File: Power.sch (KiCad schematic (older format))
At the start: 0 parts

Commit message: Understanding the Power Protection And Filtering Module
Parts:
- added C? (x2): C, symbol C
- added F? (x4): FUSE, symbol FUSE
- added L? (x2): INDUCTOR, symbol INDUCTOR
- added P?: CONN_12X2, symbol CONN_12X2
- added R?: R, symbol R
- added SW?: SWITCH_INV, symbol SWITCH_INV
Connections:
- net labels added: +12P, +12V, +3.3V, +5V, -12P, -12V, GND
- wire segments 0 -> 39

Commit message: Revisting the Current/Fan Module
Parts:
- removed F? (x4): FUSE, symbol FUSE
- added TH? (x4): THERMISTOR, symbol THERMISTOR
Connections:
- net labels added: +12C
- wire segments 39 -> 40
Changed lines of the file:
@@
 $Descr A4 11693 8268
 encoding utf-8
-Sheet 5 9
+Sheet 4 9
 Title ""
 Date ""
@@
 $EndComp
 $Comp
-L FUSE F?
-U 1 1 52F2232F
-P 3350 2100
-F 0 "F?" H 3450 2150 40  0000 C CNN
-F 1 "FUSE" H 3250 2050 40  0000 C CNN
-F 2 "" H 3350 2100 60  0000 C CNN
-F 3 "" H 3350 2100 60  0000 C CNN
-	1    3350 2100
-	1    0    0    -1
-$EndComp
-$Comp
-L FUSE F?
-U 1 1 52F2234B
-P 3950 2300
-F 0 "F?" H 4050 2350 40  0000 C CNN
-F 1 "FUSE" H 3850 2250 40  0000 C CNN
-F 2 "" H 3950 2300 60  0000 C CNN
-F 3 "" H 3950 2300 60  0000 C CNN
-	1    3950 2300
-	1    0    0    -1
-$EndComp
-$Comp
-L FUSE F?
-U 1 1 52F22356
-P 4550 2500
-F 0 "F?" H 4650 2550 40  0000 C CNN
-F 1 "FUSE" H 4450 2450 40  0000 C CNN
-F 2 "" H 4550 2500 60  0000 C CNN
-F 3 "" H 4550 2500 60  0000 C CNN
-	1    4550 2500
-	1    0    0    -1
-$EndComp
-$Comp
-L FUSE F?
-U 1 1 52F22361
-P 5150 2700
-F 0 "F?" H 5250 2750 40  0000 C CNN
-F 1 "FUSE" H 5050 2650 40  0000 C CNN
-F 2 "" H 5150 2700 60  0000 C CNN
-F 3 "" H 5150 2700 60  0000 C CNN
-	1    5150 2700
-	1    0    0    -1
-$EndComp
-$Comp
 L SWITCH_INV SW?
 U 1 1 52F2236E
@@
 	9850 3700 9850 3850
 Connection ~ 9100 3700
+Wire Wire Line
+	2950 2500 2950 1750
+Connection ~ 2950 2500
+$Comp
+L +12C #PWR?
+U 1 1 52F834A0
+P 2950 1750
+F 0 "#PWR?" H 2950 1720 30  0001 C CNN
+F 1 "+12C" H 2950 1860 40  0000 C CNN
+F 2 "" H 2950 1750 60  0000 C CNN
+F 3 "" H 2950 1750 60  0000 C CNN
+	1    2950 1750
+	1    0    0    -1
+$EndComp
+$Comp
+L THERMISTOR TH?
+U 1 1 52F839EB
+P 3350 2100
+F 0 "TH?" V 3450 2150 50  0000 C CNN
+F 1 "THERMISTOR" V 3250 2100 50  0000 C CNN
+F 2 "" H 3350 2100 60  0000 C CNN
+F 3 "" H 3350 2100 60  0000 C CNN
+	1    3350 2100
+	0    -1   -1   0
+$EndComp
+$Comp
+L THERMISTOR TH?
+U 1 1 52F83A04
+P 3950 2300
+F 0 "TH?" V 4050 2350 50  0000 C CNN
+F 1 "THERMISTOR" V 3850 2300 50  0000 C CNN
+F 2 "" H 3950 2300 60  0000 C CNN
+F 3 "" H 3950 2300 60  0000 C CNN
+	1    3950 2300
+	0    -1   -1   0
+$EndComp
+$Comp
+L THERMISTOR TH?
+U 1 1 52F83A18
+P 4550 2500
+F 0 "TH?" V 4650 2550 50  0000 C CNN
+F 1 "THERMISTOR" V 4450 2500 50  0000 C CNN
+F 2 "" H 4550 2500 60  0000 C CNN
+F 3 "" H 4550 2500 60  0000 C CNN
+	1    4550 2500
+	0    -1   -1   0
+$EndComp
+$Comp
+L THERMISTOR TH?
+U 1 1 52F83A2C
+P 5150 2700
+F 0 "TH?" V 5250 2750 50  0000 C CNN
+F 1 "THERMISTOR" V 5050 2700 50  0000 C CNN
+F 2 "" H 5150 2700 60  0000 C CNN
+F 3 "" H 5150 2700 60  0000 C CNN
+	1    5150 2700
+	0    -1   -1   0
+$EndComp
 $EndSCHEMATC

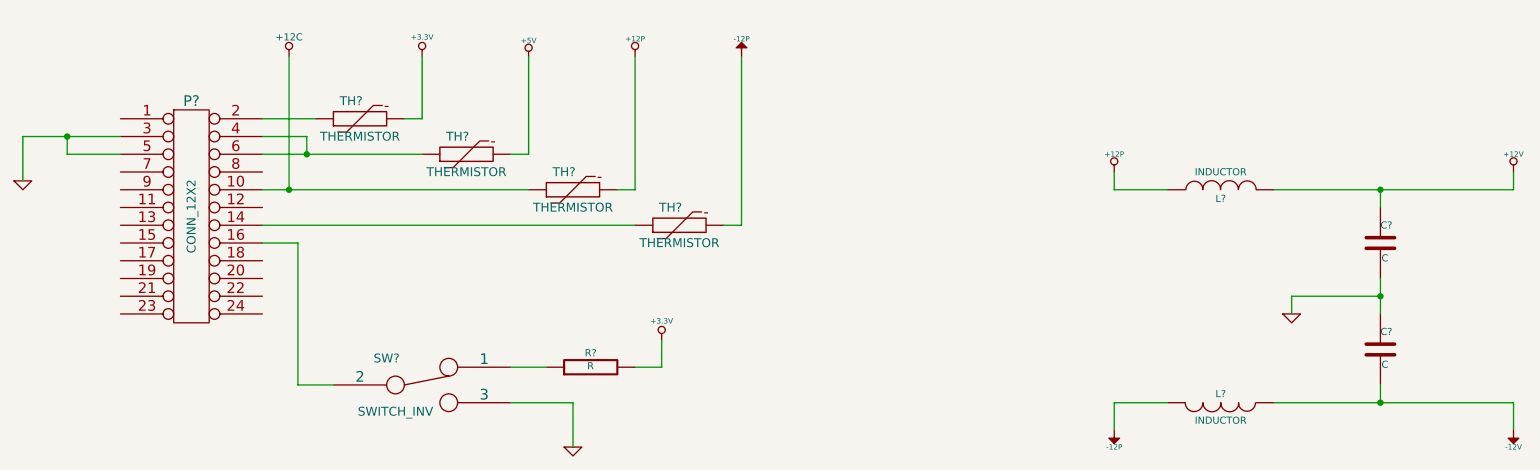
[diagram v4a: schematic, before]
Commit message: Associating and Placing the Relay Module
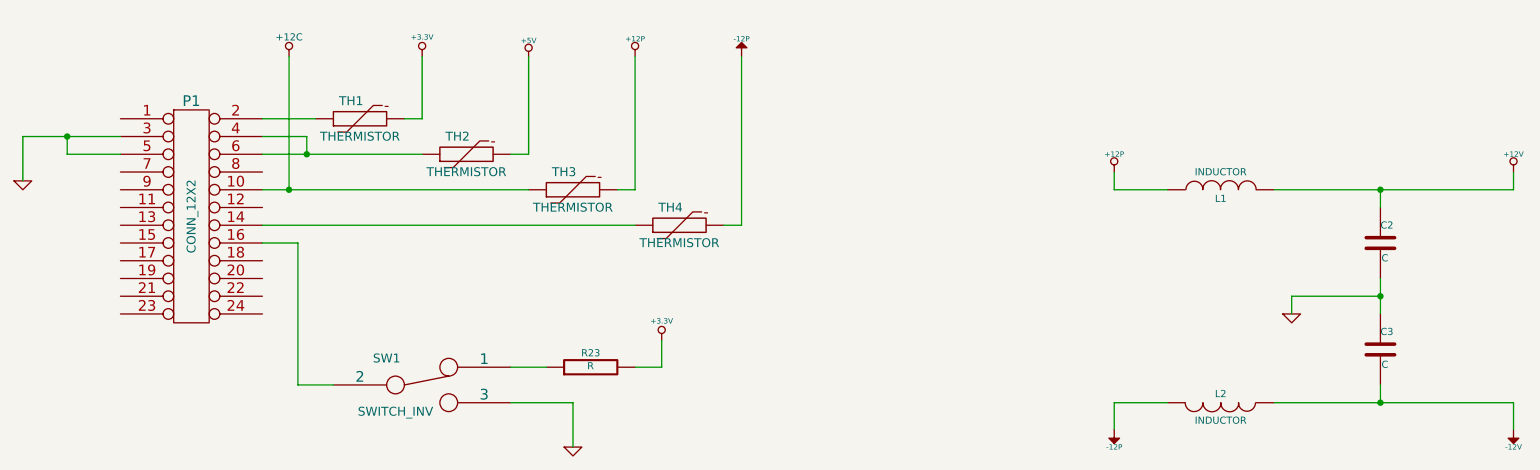
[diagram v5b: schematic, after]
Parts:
- gave numbers to parts that had none: 11
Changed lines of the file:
@@
 $EndDescr
 $Comp
-L CONN_12X2 P?
+L CONN_12X2 P1
 U 1 1 52F2195D
 P 2400 2650
-F 0 "P?" H 2400 3300 60  0000 C CNN
+F 0 "P1" H 2400 3300 60  0000 C CNN
 F 1 "CONN_12X2" V 2400 2650 50  0000 C CNN
 F 2 "" H 2400 2650 60  0000 C CNN
@@
 $EndComp
 $Comp
-L SWITCH_INV SW?
+L SWITCH_INV SW1
 U 1 1 52F2236E
 P 3700 3600
-F 0 "SW?" H 3500 3750 50  0000 C CNN
+F 0 "SW1" H 3500 3750 50  0000 C CNN
 F 1 "SWITCH_INV" H 3550 3450 50  0000 C CNN
 F 2 "" H 3700 3600 60  0000 C CNN
@@
 	2800 2100 3100 2100
 $Comp
-L +3.3V #PWR?
+L +3.3V #PWR013
 U 1 1 52F22396
 P 3700 1750
-F 0 "#PWR?" H 3700 1710 30  0001 C CNN
+F 0 "#PWR013" H 3700 1710 30  0001 C CNN
 F 1 "+3.3V" H 3700 1860 30  0000 C CNN
 F 2 "" H 3700 1750 60  0000 C CNN
@@
 Connection ~ 3050 2300
 $Comp
-L +5V #PWR?
+L +5V #PWR014
 U 1 1 52F223C7
 P 4300 1750
-F 0 "#PWR?" H 4300 1840 20  0001 C CNN
+F 0 "#PWR014" H 4300 1840 20  0001 C CNN
 F 1 "+5V" H 4300 1840 30  0000 C CNN
 F 2 "" H 4300 1750 60  0000 C CNN
@@
 	2800 2500 4300 2500
 $Comp
-L +12P #PWR?
+L +12P #PWR015
 U 1 1 52F223EF
 P 4900 1750
-F 0 "#PWR?" H 4900 1720 30  0001 C CNN
+F 0 "#PWR015" H 4900 1720 30  0001 C CNN
 F 1 "+12P" H 4900 1850 30  0000 C CNN
 F 2 "" H 4900 1750 60  0000 C CNN
@@
 	2800 2700 4900 2700
 $Comp
-L -12P #PWR?
+L -12P #PWR016
 U 1 1 52F2241B
 P 5500 1750
-F 0 "#PWR?" H 5500 1880 20  0001 C CNN
+F 0 "#PWR016" H 5500 1880 20  0001 C CNN
 F 1 "-12P" H 5500 1850 30  0000 C CNN
 F 2 "" H 5500 1750 60  0000 C CNN
@@
 	5500 2700 5400 2700
 $Comp
-L GND #PWR?
+L GND #PWR017
 U 1 1 52F227F1
 P 1450 2450
-F 0 "#PWR?" H 1450 2450 30  0001 C CNN
+F 0 "#PWR017" H 1450 2450 30  0001 C CNN
 F 1 "GND" H 1450 2380 30  0001 C CNN
 F 2 "" H 1450 2450 60  0000 C CNN
@@
 	3000 3600 3200 3600
 $Comp
-L GND #PWR?
+L GND #PWR018
 U 1 1 52F22849
 P 4550 3950
-F 0 "#PWR?" H 4550 3950 30  0001 C CNN
+F 0 "#PWR018" H 4550 3950 30  0001 C CNN
 F 1 "GND" H 4550 3880 30  0001 C CNN
 F 2 "" H 4550 3950 60  0000 C CNN
@@
 	4550 3700 4550 3950
 $Comp
-L R R?
+L R R23
 U 1 1 52F2286F
 P 4650 3500
-F 0 "R?" V 4730 3500 40  0000 C CNN
+F 0 "R23" V 4730 3500 40  0000 C CNN
 F 1 "R" V 4657 3501 40  0000 C CNN
 F 2 "" V 4580 3500 30  0000 C CNN
@@
 $EndComp
 $Comp
-L +3.3V #PWR?
+L +3.3V #PWR019
 U 1 1 52F22881
 P 5050 3350
-F 0 "#PWR?" H 5050 3310 30  0001 C CNN
+F 0 "#PWR019" H 5050 3310 30  0001 C CNN
 F 1 "+3.3V" H 5050 3460 30  0000 C CNN
 F 2 "" H 5050 3350 60  0000 C CNN
@@
 	5050 3500 5050 3350
 $Comp
-L +12P #PWR?
+L +12P #PWR020
 U 1 1 52F22A73
 P 7600 2400
-F 0 "#PWR?" H 7600 2370 30  0001 C CNN
+F 0 "#PWR020" H 7600 2370 30  0001 C CNN
 F 1 "+12P" H 7600 2500 30  0000 C CNN
 F 2 "" H 7600 2400 60  0000 C CNN
@@
 $EndComp
 $Comp
-L -12P #PWR?
+L -12P #PWR021
 U 1 1 52F22A7E
 P 7600 3850
-F 0 "#PWR?" H 7600 3980 20  0001 C CNN
+F 0 "#PWR021" H 7600 3980 20  0001 C CNN
 F 1 "-12P" H 7600 3950 30  0000 C CNN
 F 2 "" H 7600 3850 60  0000 C CNN
@@
 $EndComp
 $Comp
-L GND #PWR?
+L GND #PWR022
 U 1 1 52F22A98
 P 8600 3200
-F 0 "#PWR?" H 8600 3200 30  0001 C CNN
+F 0 "#PWR022" H 8600 3200 30  0001 C CNN
 F 1 "GND" H 8600 3130 30  0001 C CNN
 F 2 "" H 8600 3200 60  0000 C CNN
@@
 $EndComp
 $Comp
-L INDUCTOR L?
+L INDUCTOR L1
 U 1 1 52F22AA5
 P 8200 2500
-F 0 "L?" V 8150 2500 40  0000 C CNN
+F 0 "L1" V 8150 2500 40  0000 C CNN
 F 1 "INDUCTOR" V 8300 2500 40  0000 C CNN
 F 2 "" H 8200 2500 60  0000 C CNN
@@
 $EndComp
 $Comp
-L INDUCTOR L?
+L INDUCTOR L2
 U 1 1 52F22AC6
 P 8200 3700
-F 0 "L?" V 8150 3700 40  0000 C CNN
+F 0 "L2" V 8150 3700 40  0000 C CNN
 F 1 "INDUCTOR" V 8300 3700 40  0000 C CNN
 F 2 "" H 8200 3700 60  0000 C CNN
@@
 $EndComp
 $Comp
-L C C?
+L C C2
 U 1 1 52F22ADD
 P 9100 2800
-F 0 "C?" H 9100 2900 40  0000 L CNN
+F 0 "C2" H 9100 2900 40  0000 L CNN
 F 1 "C" H 9106 2715 40  0000 L CNN
 F 2 "" H 9138 2650 30  0000 C CNN
@@
 $EndComp
 $Comp
-L C C?
+L C C3
 U 1 1 52F22AEF
 P 9100 3400
-F 0 "C?" H 9100 3500 40  0000 L CNN
+F 0 "C3" H 9100 3500 40  0000 L CNN
 F 1 "C" H 9106 3315 40  0000 L CNN
 F 2 "" H 9138 3250 30  0000 C CNN
@@
 Connection ~ 9100 3100
 $Comp
-L +12V #PWR?
+L +12V #PWR023
 U 1 1 52F22BF3
 P 9850 2400
-F 0 "#PWR?" H 9850 2350 20  0001 C CNN
+F 0 "#PWR023" H 9850 2350 20  0001 C CNN
 F 1 "+12V" H 9850 2500 30  0000 C CNN
 F 2 "" H 9850 2400 60  0000 C CNN
@@
 $EndComp
 $Comp
-L -12V #PWR?
+L -12V #PWR024
 U 1 1 52F22C07
 P 9850 3850
-F 0 "#PWR?" H 9850 3980 20  0001 C CNN
+F 0 "#PWR024" H 9850 3980 20  0001 C CNN
 F 1 "-12V" H 9850 3950 30  0000 C CNN
 F 2 "" H 9850 3850 60  0000 C CNN
@@
 Connection ~ 2950 2500
 $Comp
-L +12C #PWR?
+L +12C #PWR025
 U 1 1 52F834A0
 P 2950 1750
-F 0 "#PWR?" H 2950 1720 30  0001 C CNN
+F 0 "#PWR025" H 2950 1720 30  0001 C CNN
 F 1 "+12C" H 2950 1860 40  0000 C CNN
 F 2 "" H 2950 1750 60  0000 C CNN
@@
 $EndComp
 $Comp
-L THERMISTOR TH?
+L THERMISTOR TH1
 U 1 1 52F839EB
 P 3350 2100
-F 0 "TH?" V 3450 2150 50  0000 C CNN
+F 0 "TH1" V 3450 2150 50  0000 C CNN
 F 1 "THERMISTOR" V 3250 2100 50  0000 C CNN
 F 2 "" H 3350 2100 60  0000 C CNN
@@
 $EndComp
 $Comp
-L THERMISTOR TH?
+L THERMISTOR TH2
 U 1 1 52F83A04
 P 3950 2300
-F 0 "TH?" V 4050 2350 50  0000 C CNN
+F 0 "TH2" V 4050 2350 50  0000 C CNN
 F 1 "THERMISTOR" V 3850 2300 50  0000 C CNN
 F 2 "" H 3950 2300 60  0000 C CNN
@@
 $EndComp
 $Comp
-L THERMISTOR TH?
+L THERMISTOR TH3
 U 1 1 52F83A18
 P 4550 2500
-F 0 "TH?" V 4650 2550 50  0000 C CNN
+F 0 "TH3" V 4650 2550 50  0000 C CNN
 F 1 "THERMISTOR" V 4450 2500 50  0000 C CNN
 F 2 "" H 4550 2500 60  0000 C CNN
@@
 $EndComp
 $Comp
-L THERMISTOR TH?
+L THERMISTOR TH4
 U 1 1 52F83A2C
 P 5150 2700
-F 0 "TH?" V 5250 2750 50  0000 C CNN
+F 0 "TH4" V 5250 2750 50  0000 C CNN
 F 1 "THERMISTOR" V 5050 2700 50  0000 C CNN
 F 2 "" H 5150 2700 60  0000 C CNN

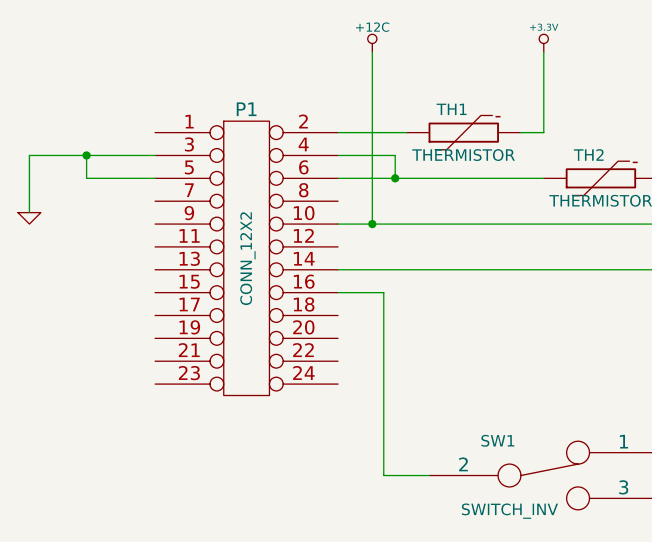
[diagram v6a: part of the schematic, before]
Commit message: Associating and Placing the Terminal/ATX Blocks
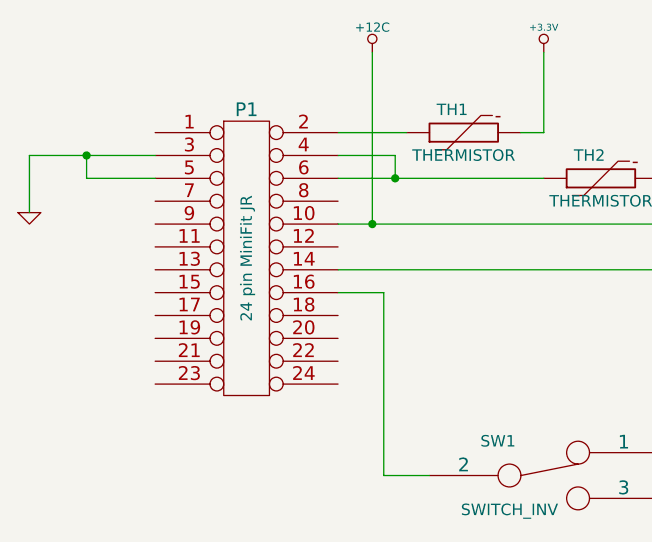
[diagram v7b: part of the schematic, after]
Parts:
- P1: value CONN_12X2 -> 24 pin MiniFit JR; MFG Name (none) -> Molex; MFG Part Number (none) -> 39-30-1240
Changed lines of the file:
@@
 P 2400 2650
 F 0 "P1" H 2400 3300 60  0000 C CNN
-F 1 "CONN_12X2" V 2400 2650 50  0000 C CNN
+F 1 "24 pin MiniFit JR" V 2400 2650 50  0000 C CNN
 F 2 "" H 2400 2650 60  0000 C CNN
 F 3 "" H 2400 2650 60  0000 C CNN
+F 4 "Molex" H 2400 2650 60  0001 C CNN "MFG Name"
+F 5 "39-30-1240" H 2400 2650 60  0001 C CNN "MFG Part Number"
 	1    2400 2650
 	1    0    0    -1
